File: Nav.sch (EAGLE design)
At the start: 33 parts, among them SW5 THAU13-AB-R, SW6 THAU13-AB-R, SW7 TVAF06-A020B-R, SW8 TVAF06-A020B-R, U4 OPA340N, U5 DRIVER-LV8548MC-AH(SOIC10), U6 I-02247_NJM2845

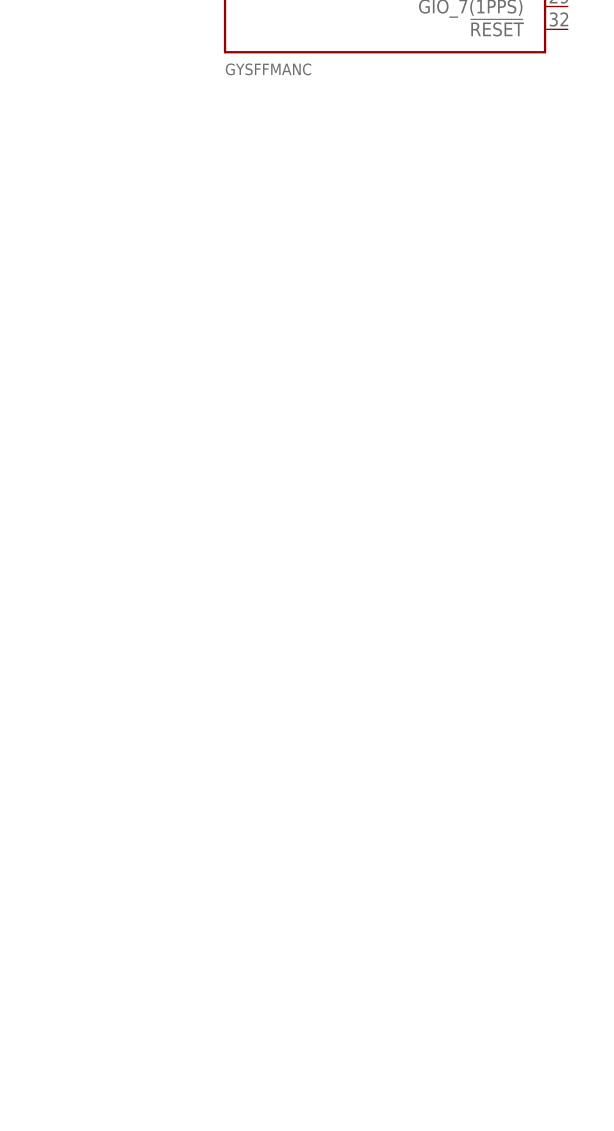
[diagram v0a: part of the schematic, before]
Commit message: Add sensors
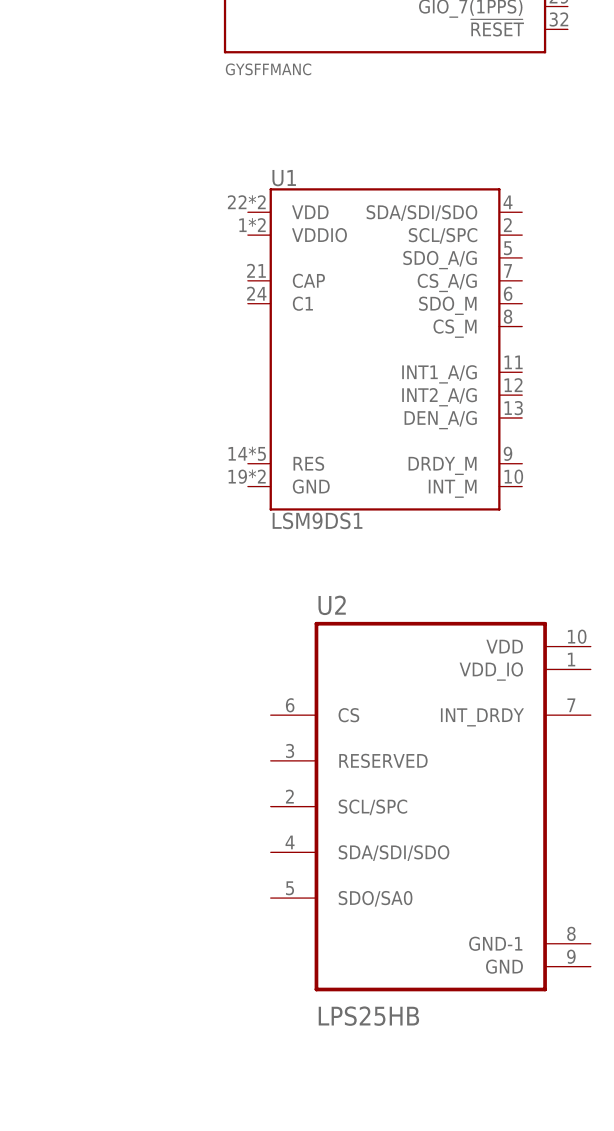
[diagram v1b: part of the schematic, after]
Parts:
- added U1: LSM9DS1, LSM9DS1:LSM9DS1
- added U2: LPS25HB, LPS25HB:LPS25HB
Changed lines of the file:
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@@
 <part name="GND42" library="supply1" library_urn="urn:adsk.eagle:library:371" deviceset="GND" device=""/>
 <part name="U$1" library="gps" deviceset="GYSFFMANC" device=""/>
+<part name="U1" library="LSM9DS1" deviceset="LSM9DS1" device=""/>
+<part name="U2" library="LPS25HB" deviceset="LPS25HB" device=""/>
 </parts>
 <sheets>
@@
 <attribute name="VALUE" x="284.48" y="114.3" size="1.27" layer="96"/>
 </instance>
+<instance part="U1" gate="G$1" x="302.26" y="83.82" smashed="yes">
+<attribute name="VALUE" x="289.56" y="64.77" size="1.778" layer="96" align="center-left"/>
+<attribute name="NAME" x="289.56" y="102.87" size="1.778" layer="95" align="center-left"/>
+</instance>
+<instance part="U2" gate="G$1" x="307.34" y="33.02" smashed="yes">
+<attribute name="NAME" x="294.64" y="54.34" size="2.0828" layer="95" ratio="10" rot="SR0"/>
+<attribute name="VALUE" x="294.64" y="8.7" size="2.0828" layer="96" ratio="10" rot="SR0"/>
+</instance>
 </instances>

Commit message: Navigation unit
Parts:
- added C1: (no value), rcl:C-EUC0603
- added C2: 10µF, rcl:C-EUC0603
- added C3, C4, C5: 0.1µF, rcl:C-EUC0603
- added C6: 0.01µF, rcl:C-EUC0603
- added J1: U.FL-R-SMT, connector:U.FL-R-SMT
- added R1, R2: 10k, rcl:R-US_R0603
- added SC: DCK-3R3E, capacitors:DCK-3R3E
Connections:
- new net 1PPS: U$1.GIO_7(1PPS)
- new net ANT: J1.ANT, U$1.ANT
- new net GPS_!RESET!: U$1.!RESET!
- new net GPS_RTX: U$1.UART_TXD
- new net GPS_TRX: U$1.UART_RXD
- new net N$1: SC.+, U$1.VDD3V3_BACKUP
- new net N$4: C6.1, U1.C1
- new net N$6: C5.1, U1.CAP
- net GND: now also C1.2, C2.2, C3.2, C4.2, C5.2, C6.2, J1.P$2, SC.-, U$1.GND, U1.GND, U1.RES, U2.GND, U2.GND-1, U2.RESERVED, U2.SDO/SA0
- net I2C_SCL: now also R1.1, U1.SCL/SPC, U2.SCL/SPC
- net I2C_SDA: now also R2.1, U1.SDA/SDI/SDO, U2.SDA/SDI/SDO
- net VDD: now also C1.1, C2.1, C3.1, C4.1, R1.2, R2.2, U$1.VDD3V3, U1.VDD, U1.VDDIO, U2.CS, U2.VDD, U2.VDD_IO
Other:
- moved on the sheet: U$1, U1

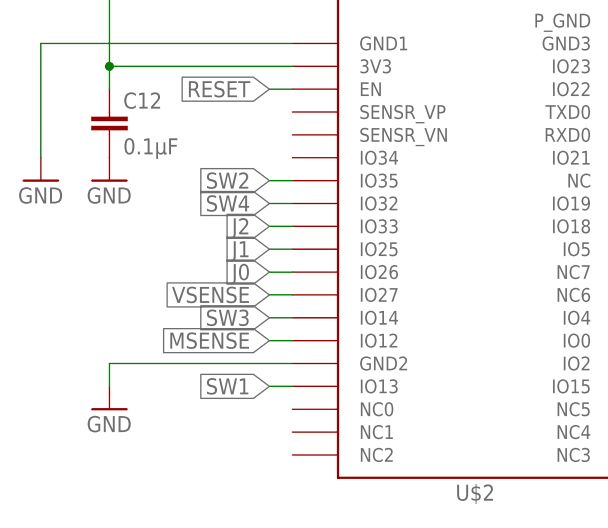
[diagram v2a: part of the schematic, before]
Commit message: Fix analog input pins
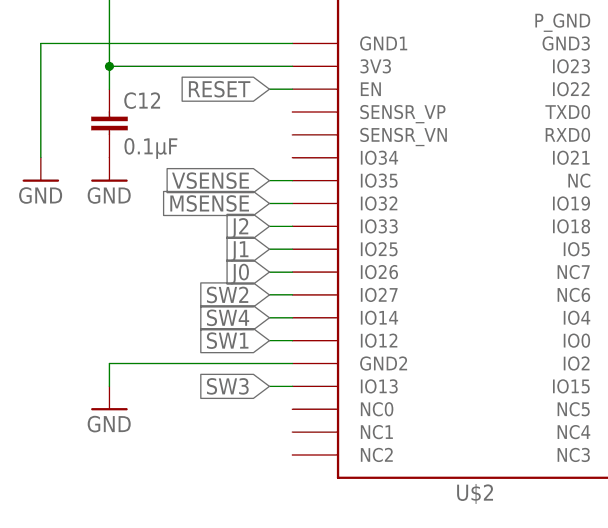
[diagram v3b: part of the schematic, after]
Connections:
- net MSENSE: now also U$2.IO32; no longer U$2.IO12
- net SW1: now also U$2.IO12; no longer U$2.IO13
- net SW2: now also U$2.IO27; no longer U$2.IO35
- net SW3: now also U$2.IO13; no longer U$2.IO14
- net SW4: now also U$2.IO14; no longer U$2.IO32
- net VSENSE: now also U$2.IO35; no longer U$2.IO27
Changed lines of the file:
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@@
 </segment>
 <segment>
-<pinref part="U$2" gate="G$1" pin="IO12"/>
-<wire x1="30.48" y1="17.78" x2="27.94" y2="17.78" width="0.1524" layer="91"/>
-<label x="27.94" y="17.78" size="1.778" layer="95" rot="R180" xref="yes"/>
+<pinref part="U$2" gate="G$1" pin="IO32"/>
+<wire x1="30.48" y1="33.02" x2="27.94" y2="33.02" width="0.1524" layer="91"/>
+<label x="27.94" y="33.02" size="1.778" layer="95" rot="R180" xref="yes"/>
 </segment>
 </net>
@@
 </segment>
 <segment>
-<pinref part="U$2" gate="G$1" pin="IO27"/>
-<wire x1="30.48" y1="22.86" x2="27.94" y2="22.86" width="0.1524" layer="91"/>
-<label x="27.94" y="22.86" size="1.778" layer="95" rot="R180" xref="yes"/>
+<pinref part="U$2" gate="G$1" pin="IO35"/>
+<wire x1="30.48" y1="35.56" x2="27.94" y2="35.56" width="0.1524" layer="91"/>
+<label x="27.94" y="35.56" size="1.778" layer="95" rot="R180" xref="yes"/>
 </segment>
 </net>
@@
 </segment>
 <segment>
-<pinref part="U$2" gate="G$1" pin="IO35"/>
-<wire x1="30.48" y1="35.56" x2="27.94" y2="35.56" width="0.1524" layer="91"/>
-<label x="27.94" y="35.56" size="1.778" layer="95" rot="R180" xref="yes"/>
+<pinref part="U$2" gate="G$1" pin="IO27"/>
+<wire x1="30.48" y1="22.86" x2="27.94" y2="22.86" width="0.1524" layer="91"/>
+<label x="27.94" y="22.86" size="1.778" layer="95" rot="R180" xref="yes"/>
 </segment>
 </net>
@@
 </segment>
 <segment>
+<pinref part="U$2" gate="G$1" pin="IO13"/>
+<wire x1="30.48" y1="12.7" x2="27.94" y2="12.7" width="0.1524" layer="91"/>
+<label x="27.94" y="12.7" size="1.778" layer="95" rot="R180" xref="yes"/>
+</segment>
+</net>
+<net name="SW4" class="0">
+<segment>
+<pinref part="SW8" gate="G$1" pin="A"/>
+<wire x1="218.44" y1="83.82" x2="215.9" y2="83.82" width="0.1524" layer="91"/>
+<label x="215.9" y="83.82" size="1.778" layer="95" rot="R180" xref="yes"/>
+</segment>
+<segment>
 <pinref part="U$2" gate="G$1" pin="IO14"/>
 <wire x1="30.48" y1="20.32" x2="27.94" y2="20.32" width="0.1524" layer="91"/>
@@
 </segment>
 </net>
-<net name="SW4" class="0">
-<segment>
-<pinref part="SW8" gate="G$1" pin="A"/>
-<wire x1="218.44" y1="83.82" x2="215.9" y2="83.82" width="0.1524" layer="91"/>
-<label x="215.9" y="83.82" size="1.778" layer="95" rot="R180" xref="yes"/>
-</segment>
-<segment>
-<pinref part="U$2" gate="G$1" pin="IO32"/>
-<wire x1="30.48" y1="33.02" x2="27.94" y2="33.02" width="0.1524" layer="91"/>
-<label x="27.94" y="33.02" size="1.778" layer="95" rot="R180" xref="yes"/>
-</segment>
-</net>
 <net name="SW1" class="0">
 <segment>
@@
 </segment>
 <segment>
-<pinref part="U$2" gate="G$1" pin="IO13"/>
-<wire x1="30.48" y1="12.7" x2="27.94" y2="12.7" width="0.1524" layer="91"/>
-<label x="27.94" y="12.7" size="1.778" layer="95" rot="R180" xref="yes"/>
-</segment>
-</net>
+<pinref part="U$2" gate="G$1" pin="IO12"/>
+<wire x1="30.48" y1="17.78" x2="27.94" y2="17.78" width="0.1524" layer="91"/>
+<label x="27.94" y="17.78" size="1.778" layer="95" rot="R180" xref="yes"/>
+</segment>
+</net>

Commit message: reduce switch pins
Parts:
- removed C10: 2.2µF, rcl:C-EUC0603
- removed C11: 220µF, rcl:CPOL-EUUD-6,3X7,7
- removed C12, C7: 0.1µF, rcl:C-EUC0603
- removed C8: 1µF, rcl:C-EUC0603
- removed C9: 0.33µF, rcl:C-EUC0603
- removed J3, J4, J5: (no value), jumper:SJ
- removed R10, R8: 1k, rcl:R-US_R0603
- removed R11, R13, R14, R9: 100k, rcl:R-US_R0603
- removed R12: 200k, rcl:R-US_R0603
- removed U$2: ESP32-WROVER-E, esp32:ESP32-WROVER-E
- removed U4: OPA340N, burr-brown:OPA340N
- removed U5: DRIVER-LV8548MC-AH(SOIC10), DRIVER-LV8548MC-AH_SOIC10_:DRIVER-LV8548MC-AH(SOIC10)
- added C13, C18: 0.1µF, rcl:C-EUC0603
- added C14: 1µF, rcl:C-EUC0603
- added C15: 0.33µF, rcl:C-EUC0603
- added C16: 2.2µF, rcl:C-EUC0603
- added C17: 220µF, rcl:CPOL-EUUD-6,3X7,7
- added R15, R17: 1k, rcl:R-US_R0603
- added R16, R18, R20, R21: 100k, rcl:R-US_R0603
- added R19: 200k, rcl:R-US_R0603
- added R22, R23, R24, R25, R26: (no value), rcl:R-US_R0603
- added U$7: P2_5_1.27, pins:P2_5_1.27
- added U7: DRIVER-LV8548MC-AH(SOIC10), DRIVER-LV8548MC-AH_SOIC10_:DRIVER-LV8548MC-AH(SOIC10)
- added U8: I-02247_NJM2845, akizuki:I-02247_NJM2845
- U$4: value SS12D01GX -> ESP32-WROVER-E; device switches:SS12D01GX -> esp32:ESP32-WROVER-E
- U$5: value P2_5_1.27 -> SS12D01GX; device pins:P2_5_1.27 -> switches:SS12D01GX
- U6: value I-02247_NJM2845 -> OPA340N; device akizuki:I-02247_NJM2845 -> burr-brown:OPA340N
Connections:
- removed net J0: J3.1, U$2.IO26
- removed net J1: J4.1, U$2.IO25
- removed net J2: J5.1, U$2.IO33
- removed net N$10: R14.1, T1.G, U$4.A
- removed net N$5: HUSE1.P2, R14.2, T1.S
- removed net N$8: R8.2, R9.1, U4.-IN
- removed net N$9: R10.2, R11.1, U4.+IN
- removed net SPI_CLK: U$2.IO18
- removed net SPI_CS: U$2.IO5
- removed net SPI_MISO: U$2.IO19
- removed net SW1: SW6.A, U$2.IO12
- removed net SW2: SW5.A, U$2.IO27
- removed net SW3: SW7.A, U$2.IO13
- removed net SW4: SW8.A, U$2.IO14
- new net N$13: HUSE1.P2, R21.2, T1.S
- new net N$14: R15.2, R16.1, U6.-IN
- new net N$15: R17.2, R18.1, U6.+IN
- new net N$16: R21.1, T1.G, U$5.A
- new net N$19: R24.1, R25.2, SW5.A, SW7.B
- new net N$20: R23.1, R24.2, SW6.B, SW7.A
- new net N$21: R25.1, R26.2, SW5.B, SW8.A
- new net SW: R22.1, R23.2, SW6.A, U$4.IO34
- net 1: now also U$7.7; no longer U$5.7
- net 1PPS: now also U$4.IO26
- net 2: now also U$7.8; no longer U$5.8
- net 3: now also U$7.9; no longer U$5.9
- net 4: now also U$7.10; no longer U$5.10
- net GND: now also C13.2, C14.1, C15.2, C16.2, C17.-, C18.2, R15.1, R18.2, R20.1, R26.1, U$4.GND1, U$4.GND2, U$4.GND3, U$4.P_GND, U$5.C, U$7.2, U6.V-, U8.GND; no longer C10.2, C11.-, C12.2, C7.2, C8.1, C9.2, J3.2, J4.2, J5.2, R11.2, R13.1, R8.1, SW5.B, SW6.B, SW7.B, U$2.GND1, U$2.GND2, U$2.GND3, U$2.P_GND, U$4.C, U$5.2, U4.V-, U6.GND
- net GPS_!RESET!: now also U$4.IO27
- net GPS_RTX: now also U$4.IO25
- net GPS_TRX: now also U$4.IO5
- net I2C_SCL: now also U$4.IO22; no longer U$2.IO22
- net I2C_SDA: now also U$4.IO21; no longer U$2.IO21
- net LED: now also U$4.IO2; no longer U$2.IO2
- net M1: now also U7.OUT1, U7.OUT3; no longer U5.OUT1, U5.OUT3
- net M2: now also U7.OUT2, U7.OUT4; no longer U5.OUT2, U5.OUT4
- net MC1: now also U$4.IO15, U7.INT1, U7.INT3; no longer U$2.IO15, U5.INT1, U5.INT3
- net MC2: now also U$4.IO4, U7.INT2, U7.INT4; no longer U$2.IO4, U5.INT2, U5.INT4
- net MGND: now also R17.1, U7.GND; no longer R10.1, U5.GND
- net MSENSE: now also R16.2, U$4.IO32, U6.OUT; no longer R9.2, U$2.IO32, U4.OUT
- net PRG: now also U$4.IO0, U$7.4; no longer U$2.IO0, U$5.4
- net RESET: now also U$4.EN, U$7.3; no longer U$2.EN, U$5.3
- net RX: now also U$4.RXD0, U$7.6; no longer U$2.RXD0, U$5.6
- net TX: now also U$4.TXD0, U$7.5; no longer U$2.TXD0, U$5.5
- net VCC: now also C14.2, C15.1, R19.2, U7.VCC, U8.VIN; no longer C8.2, C9.1, R12.2, U5.VCC, U6.VIN
- net VDD: now also C13.1, C16.1, C17.+, C18.1, R22.2, U$4.3V3, U$7.1, U6.V+, U8.VOUT; no longer C10.1, C11.+, C12.1, C7.1, U$2.3V3, U$5.1, U4.V+, U6.VOUT
- net VSENSE: now also R19.1, R20.2, U$4.IO35; no longer R12.1, R13.2, U$2.IO35
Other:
- note added: "Limit Switches & Push Switches"
- note removed: "Jumper Pads"
- note removed: "Limit Switches"
- note removed: "Push Switches"
- moved on the sheet: C1, C2, C3, C4, C5, C6, HUSE1, J1, LED4, LED5, LED6, R1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

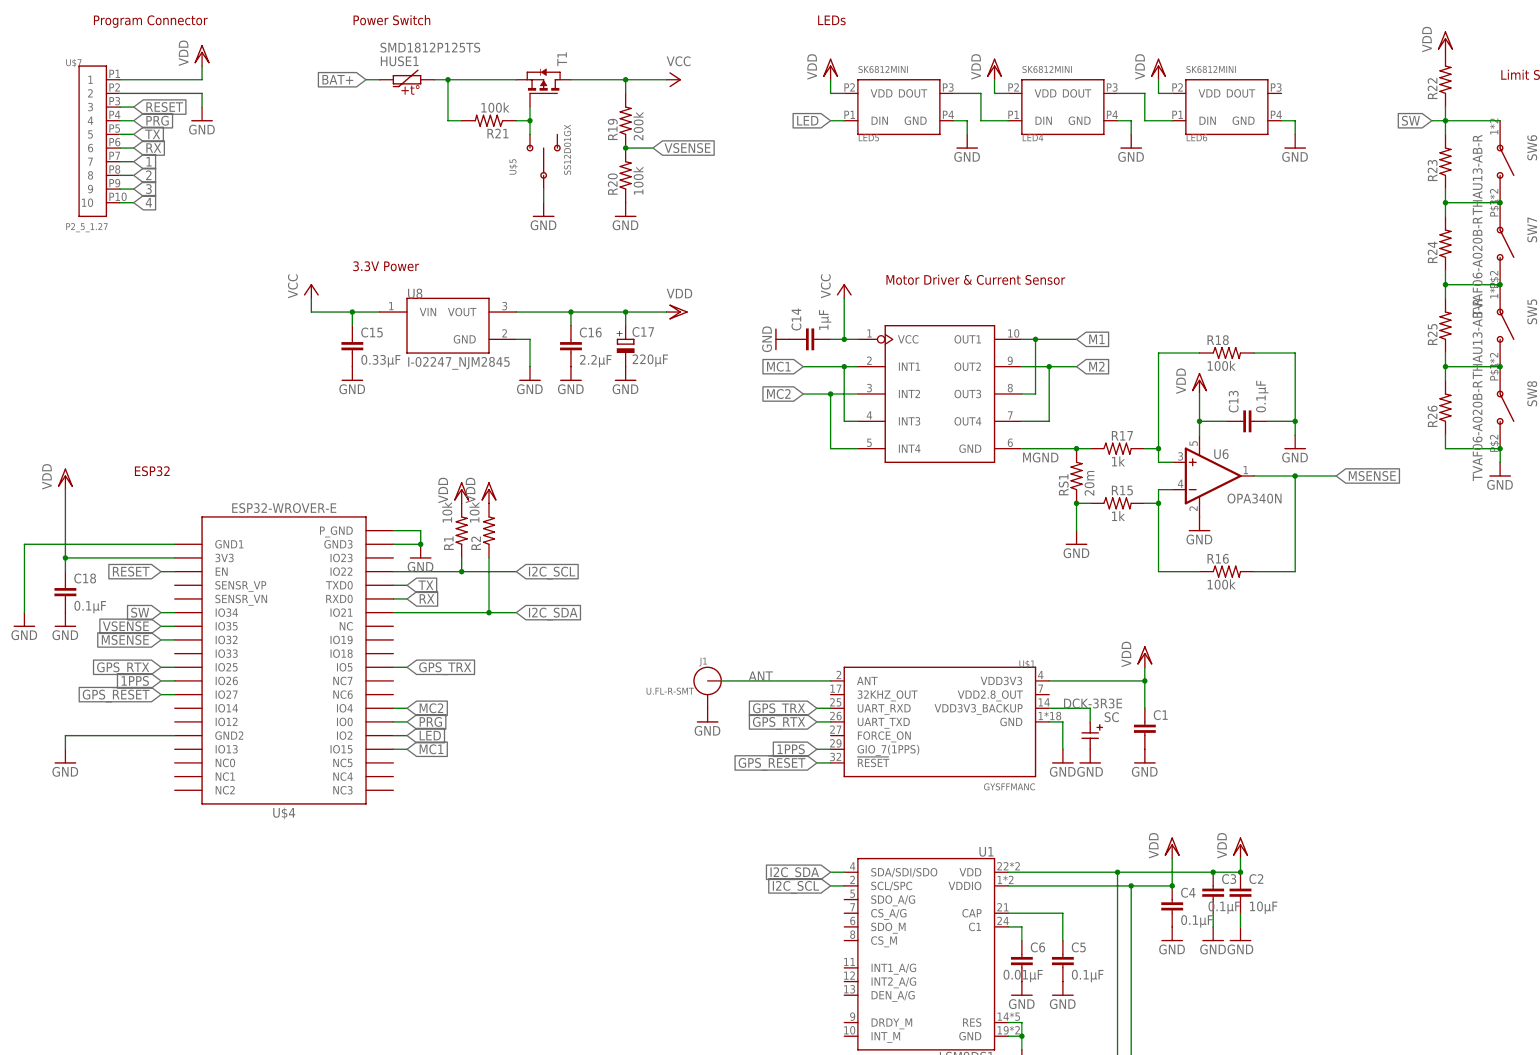
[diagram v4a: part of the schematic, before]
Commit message: change parts name
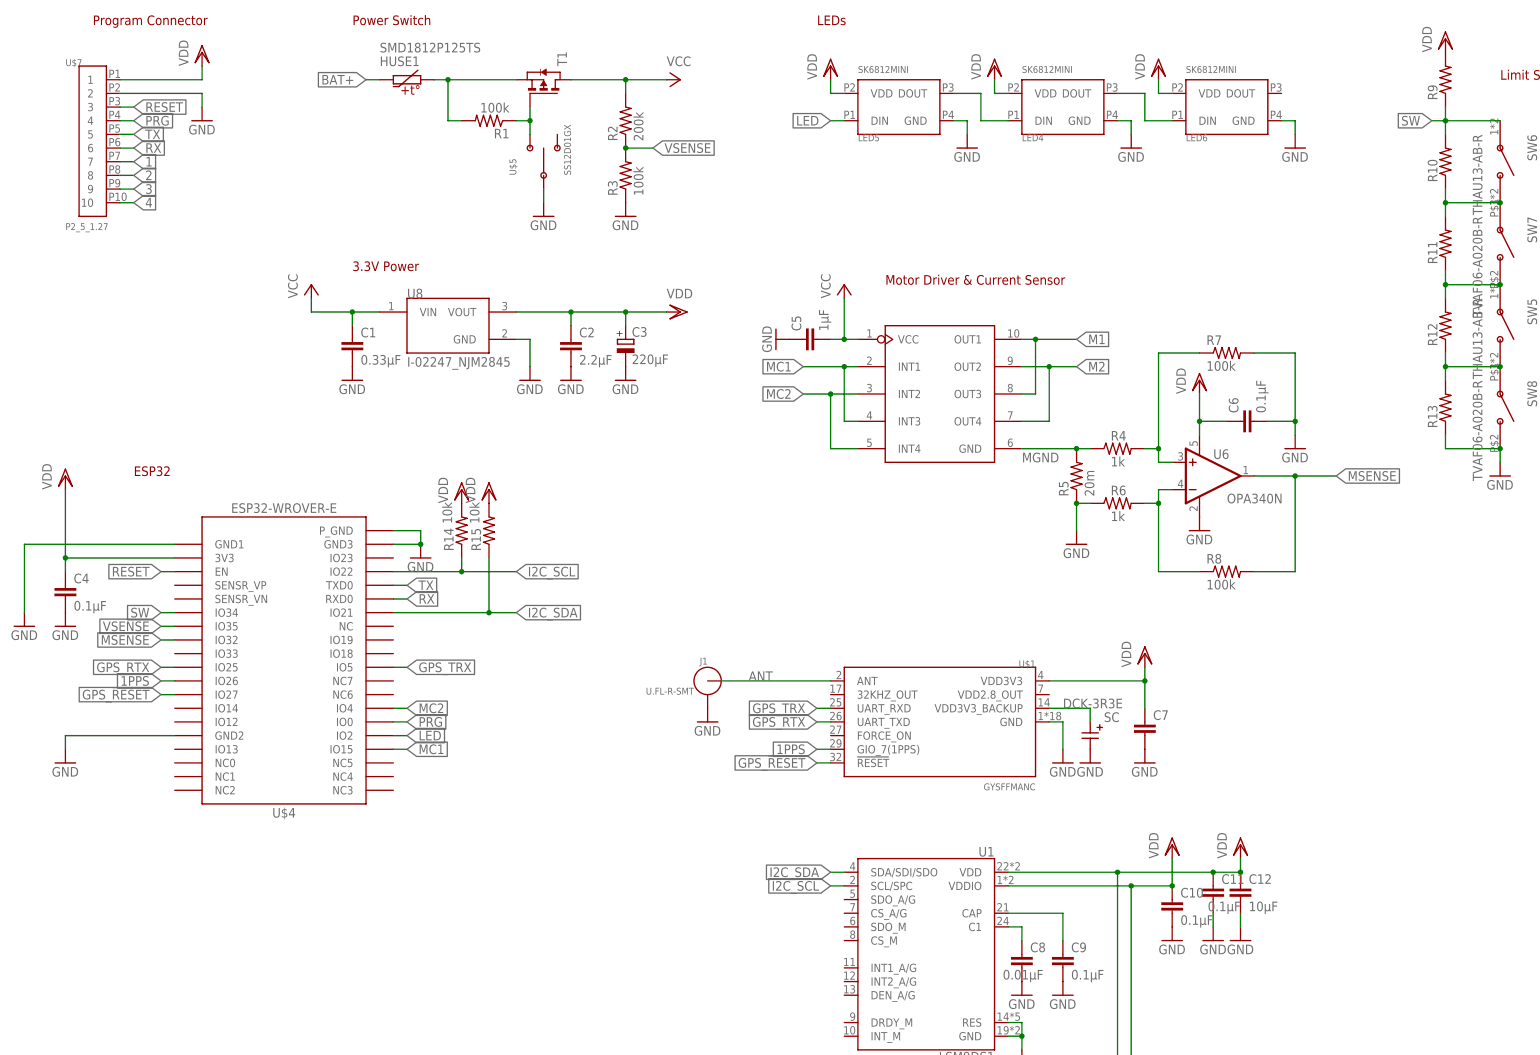
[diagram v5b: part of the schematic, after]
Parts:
- removed C13, C18: 0.1µF, rcl:C-EUC0603
- removed C14: 1µF, rcl:C-EUC0603
- removed C15: 0.33µF, rcl:C-EUC0603
- removed C16: 2.2µF, rcl:C-EUC0603
- removed C17: 220µF, rcl:CPOL-EUUD-6,3X7,7
- removed R19: 200k, rcl:R-US_R0603
- removed R21: 100k, rcl:R-US_R0603
- added C10, C11, C9: 0.1µF, rcl:C-EUC0603
- added C12: 10µF, rcl:C-EUC0603
- added C7: (no value), rcl:C-EUC0603
- added C8: 0.01µF, rcl:C-EUC0603
- added R14: 10k, rcl:R-US_R0603
- added R6: 1k, rcl:R-US_R0603
- C1: value (none) -> 0.33µF
- C2: value 10µF -> 2.2µF
- C3: value 0.1µF -> 220µF; device rcl:C-EUC0603 -> rcl:CPOL-EUUD-6,3X7,7
- C5: value 0.1µF -> 1µF
- C6: value 0.01µF -> 0.1µF
- R1: value 10k -> 100k
- R15: value 1k -> 10k
- R2: value 10k -> 200k
- renumbered R16 to R8, R17 to R4, R18 to R7, R20 to R3, R22 to R9, R23 to R10, R24 to R11, R25 to R12, R26 to R13, RS1 to R5
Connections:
- net GND: now also C10.2, C11.2, C12.2, C3.-, C5.1, C7.2, C8.2, C9.2, R6.1; no longer C13.2, C14.1, C15.2, C16.2, C17.-, C18.2, C3.2, C5.2, R15.1
- net I2C_SCL: now also R14.1; no longer R1.1
- net I2C_SDA: now also R15.1; no longer R2.1
- net N$13: now also R1.2; no longer R21.2
- net N$14: now also R6.2; no longer R15.2
- net N$16: now also R1.1; no longer R21.1
- net N$4: now also C8.1; no longer C6.1
- net N$6: now also C9.1; no longer C5.1
- net VCC: now also C1.1, C5.2, R2.2; no longer C14.2, C15.1, R19.2
- net VDD: now also C10.1, C11.1, C12.1, C3.+, C6.1, C7.1, R14.2, R15.2; no longer C1.1, C13.1, C16.1, C17.+, C18.1, C3.1, R1.2, R2.2
- net VSENSE: now also R2.1; no longer R19.1
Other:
- moved on the sheet: C1, C2, C4, C5, C6, R1, R15, R2
